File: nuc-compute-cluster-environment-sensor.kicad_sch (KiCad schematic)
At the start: 31 parts

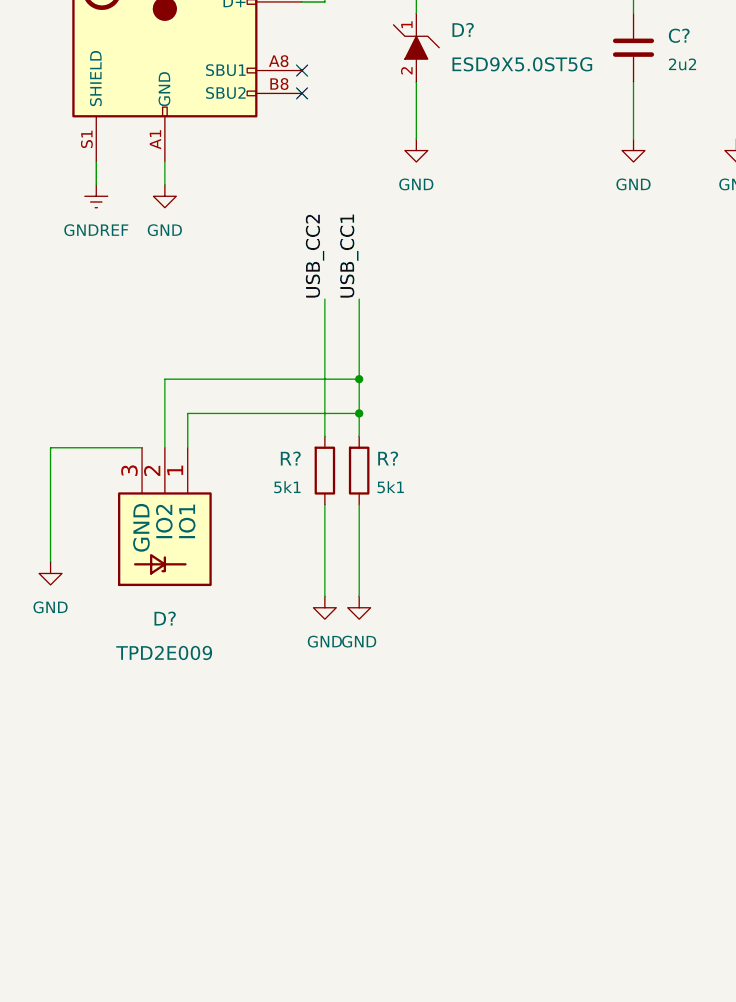
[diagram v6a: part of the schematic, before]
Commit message: [#39832] SCH: Add parallel 100n cap and 1M resistor to connect USB-C GND & Shield, as DNP for now
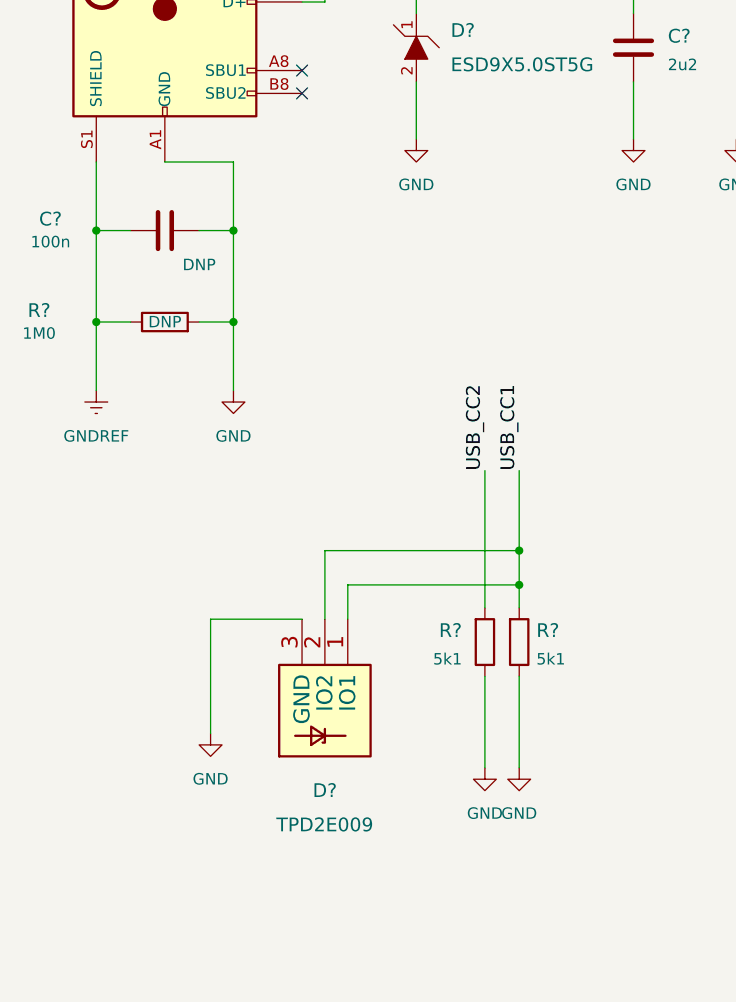
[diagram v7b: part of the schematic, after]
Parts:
- added C?: C_100n_0402, antmicro-footprints:0402-cap, symbol antmicroCapacitors0402:C_100n_0402
- added R?: R_1M0_0402, antmicro-footprints:0402-res, symbol antmicroResistors0402:R_1M0_0402
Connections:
- net GND: now also C?.2, R?.2
- net GNDREF: now also C?.1, R?.1
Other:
- moved on the sheet: D?, R?

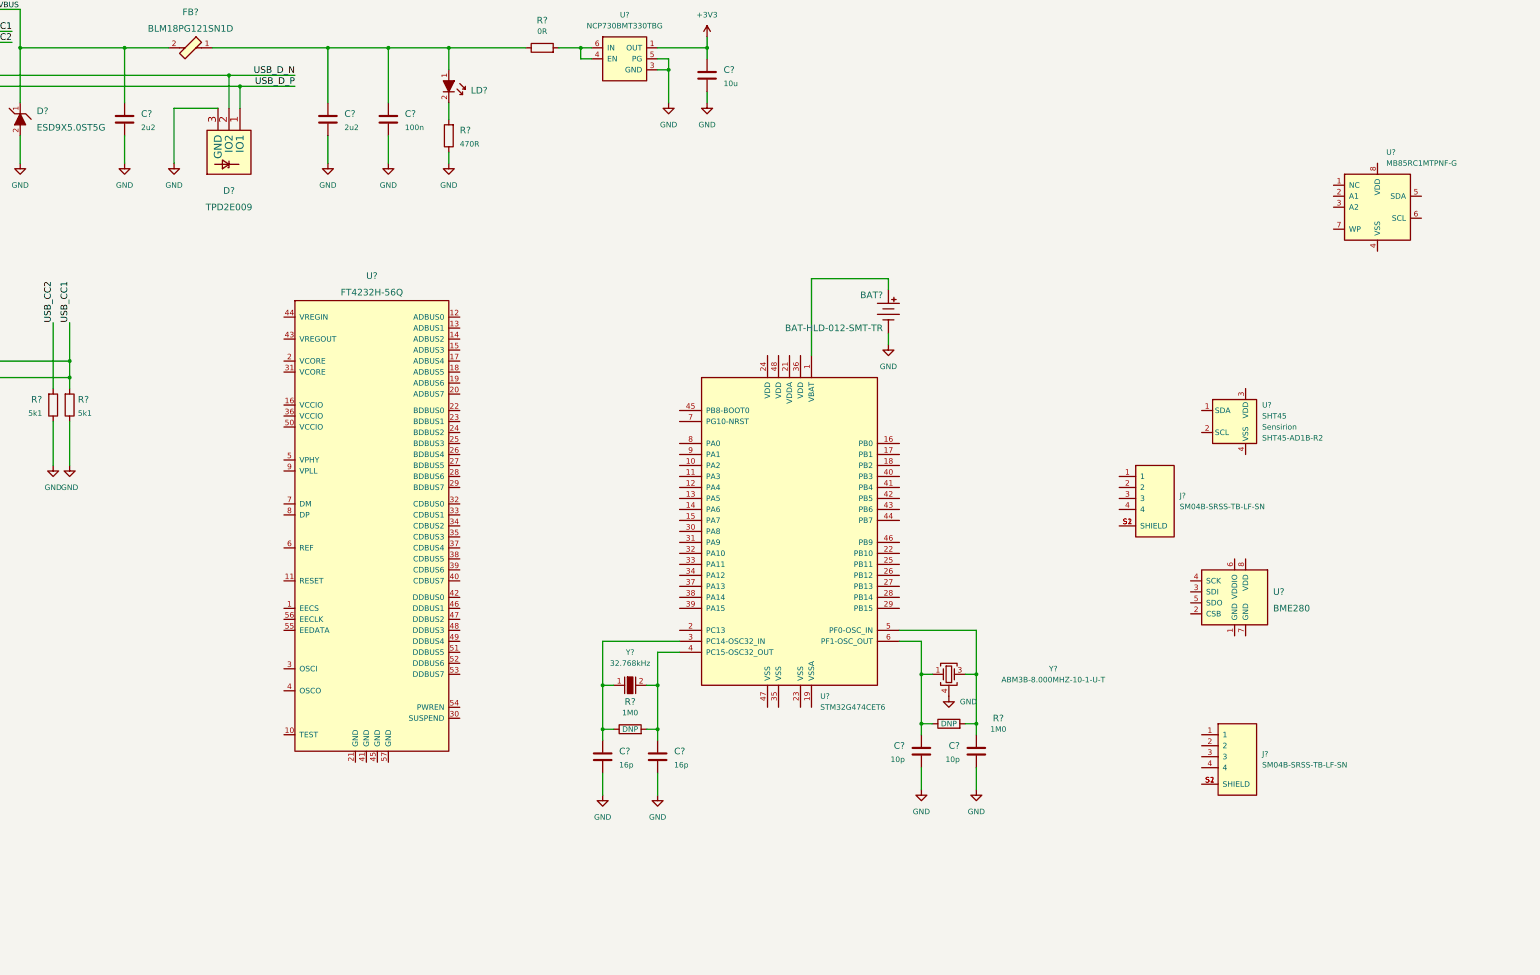
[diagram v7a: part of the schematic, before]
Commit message: [#39832] SCH: Wire up STM32 according to Default Zephyr Peripheral Mapping & datasheet, wire up SHT45 & more
Default Zephyr Peripheral Mapping listed at:
https://docs.zephyrproject.org/3.1.0/boards/arm/nucleo_g474re/doc/index.html#default-zephyr-peripheral-mapping

Full changelog:
- To STM32: Wire up VDD & VDDA, I2C_1, JTAG/SWD, LPUART_1, NRST as global labels
- Add LD2 Zephyr User LED circuit to STM32
- Add 100n decoupling capacitors
- Wire up MB85.. FRAM
- Change CC resistors to 0402 size
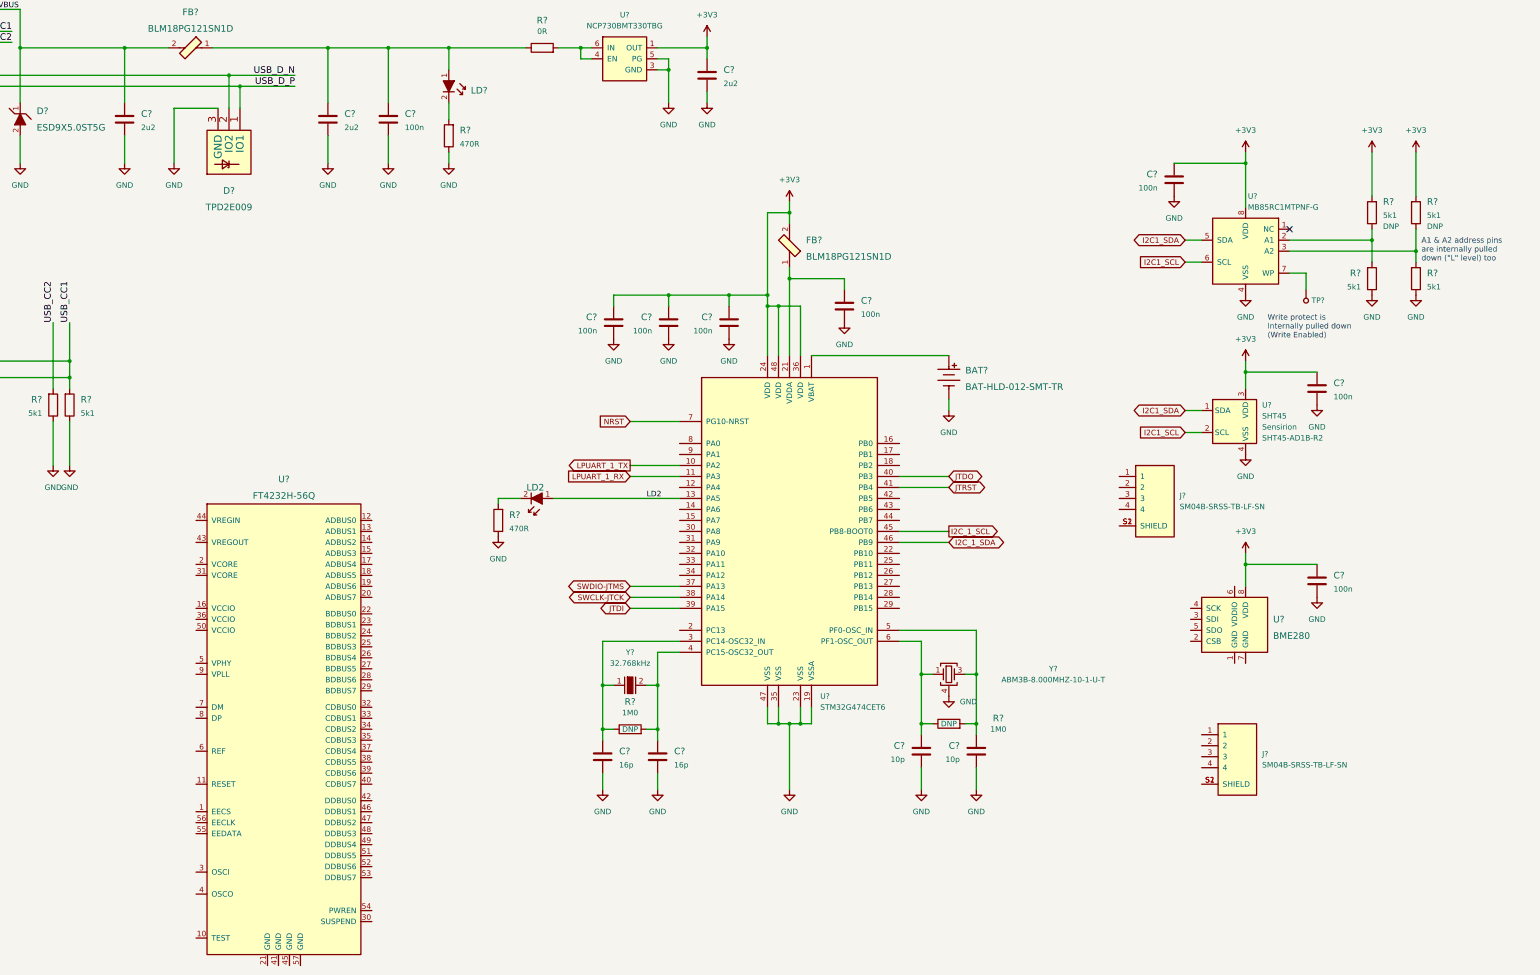
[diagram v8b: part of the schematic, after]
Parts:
- added C? (x7): C_100n_0402, antmicro-footprints:0402-cap, symbol antmicroCapacitors0402:C_100n_0402
- added FB?: BLM18PG121SN1D, antmicro-footprints:0603-res, symbol antmicroFerriteBeadsandChips:BLM18PG121SN1D
- added LD2: LG_L29K-G2J1-24-Z, antmicro-footprints:LED_0603, symbol antmicroLEDIndicationDiscrete:KP-1608ZGC
- added R? (x4): R_5k1_0402, antmicro-footprints:0402-res, symbol antmicroResistors0402:R_5k1_0402
- added R?: R_470R_0402, antmicro-footprints:0402-res, symbol antmicroResistors0402:R_470R_0402
- added TP?: TP_SMD1MM, antmicro-footprints:Testpoint_smd_1mm, symbol antmicroTestPoints:TP_SMD1MM
- C?: value C_10u_0402 -> C_2u2_0402; symbol antmicroCapacitors0402:C_10u_0402 -> antmicroCapacitors0402:C_2u2_0402; MPN CC0402MRX5R5BB106 -> C1005X5R1A225K050BC; Manufacturer YAGEO -> TDK; Val 10u -> 2u2
- R? (x2): value R_5k1_0603 -> R_5k1_0402; footprint antmicro-footprints:0603-res -> antmicro-footprints:0402-res; symbol antmicroResistors0603:R_5k1_0603 -> antmicroResistors0402:R_5k1_0402; MPN CRCW06035K10FKEA -> SFR01MZPJ512; Manufacturer Vishay -> ROHM Semiconductor
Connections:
- net +3V3: now also U?.24 (VDD), U?.3 (VDD), U?.36 (VDD), U?.48 (VDD), U?.8 (VDD), U?.8 (VDD), C?.2, C?.2, C?.2, C?.2, C?.2, C?.2, FB?.2, R?.2, R?.2
- net GND: now also U?.19 (VSSA), U?.23 (VSS), U?.35 (VSS), U?.4 (VSS), U?.4 (VSS), U?.47 (VSS), C?.1, C?.1, C?.1, C?.1, C?.1, C?.1, C?.1, R?.1, R?.1, R?.1
- net LPUART_1_TX: now reaches U?.10 (PA2)
- net LPUART_1_RX: now reaches U?.11 (PA3)
- net LD2: now reaches U?.13 (PA5)
- net LD2: now also LD2.1
- net at U?.21 (VDDA): now also C?.2, FB?.1
- net SWDIO-JTMS: now reaches U?.37 (PA13)
- net SWCLK-JTCK: now reaches U?.38 (PA14)
- net JTDI: now reaches U?.39 (PA15)
- net JTDO: now reaches U?.40 (PB3)
- net JTRST: now reaches U?.41 (PB4)
- net I2C_1_SCL: now reaches U?.45 (PB8-BOOT0)
- net I2C_1_SDA: now reaches U?.46 (PB9)
- net NRST: now reaches U?.7 (PG10-NRST)
- net at U?.2 (A1): now also R?.1, R?.2
- net at U?.3 (A2): now also R?.1, R?.2
- net I2C1_SDA: now reaches U?.5 (SDA)
- net I2C1_SDA: now also U?.1 (SDA)
- net I2C1_SCL: now reaches U?.6 (SCL)
- net I2C1_SCL: now also U?.2 (SCL)
- net at U?.7 (WP): now also TP?.1
- new net: LD2.2, R?.2
- no-connect marks 2 -> 3
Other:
- note added: "A1 & A2 address pins are internally pulled down ("L" level) too"
- note added: "Write protect is internally pulled down (Write Enabled)"
- moved on the sheet: BAT?, U?
